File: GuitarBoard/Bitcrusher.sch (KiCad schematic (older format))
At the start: 20 parts, among them IC1 CD4069UBE, Q6 2N3904

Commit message: Finalized new guitar board
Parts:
- C10, C13: footprint Capacitor_THT:CP_Axial_L10.0mm_D6.0mm_P15.00mm_Horizontal -> Capacitor_THT:CP_Radial_D6.3mm_P2.50mm
- C11, C12, C6, C7, C8, C9: footprint libraries:C_Flat_L7.2_H6.5 -> Capacitor_THT:C_Rect_L7.2mm_W2.5mm_P5.00mm_FKS2_FKP2_MKS2_MKP2
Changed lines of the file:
@@
 F 0 "C6" V 798 2550 50  0000 C CNN
 F 1 "0.1uF" V 889 2550 50  0000 C CNN
-F 2 "libraries:C_Flat_L7.2_H6.5" H 1088 2400 50  0001 C CNN
+F 2 "Capacitor_THT:C_Rect_L7.2mm_W2.5mm_P5.00mm_FKS2_FKP2_MKS2_MKP2" H 1088 2400 50  0001 C CNN
 F 3 "~" H 1050 2550 50  0001 C CNN
 	1    1050 2550
@@
 F 0 "C7" V 1298 2000 50  0000 C CNN
 F 1 "2200pF" V 1389 2000 50  0000 C CNN
-F 2 "libraries:C_Flat_L7.2_H6.5" H 1588 1850 50  0001 C CNN
+F 2 "Capacitor_THT:C_Rect_L7.2mm_W2.5mm_P5.00mm_FKS2_FKP2_MKS2_MKP2" H 1588 1850 50  0001 C CNN
 F 3 "~" H 1550 2000 50  0001 C CNN
 	1    1550 2000
@@
 F 0 "C8" V 1798 2550 50  0000 C CNN
 F 1 "0.1uF" V 1889 2550 50  0000 C CNN
-F 2 "libraries:C_Flat_L7.2_H6.5" H 2088 2400 50  0001 C CNN
+F 2 "Capacitor_THT:C_Rect_L7.2mm_W2.5mm_P5.00mm_FKS2_FKP2_MKS2_MKP2" H 2088 2400 50  0001 C CNN
 F 3 "~" H 2050 2550 50  0001 C CNN
 	1    2050 2550
@@
 F 0 "C9" V 2298 2000 50  0000 C CNN
 F 1 "4700pF" V 2389 2000 50  0000 C CNN
-F 2 "libraries:C_Flat_L7.2_H6.5" H 2588 1850 50  0001 C CNN
+F 2 "Capacitor_THT:C_Rect_L7.2mm_W2.5mm_P5.00mm_FKS2_FKP2_MKS2_MKP2" H 2588 1850 50  0001 C CNN
 F 3 "~" H 2550 2000 50  0001 C CNN
 	1    2550 2000
@@
 F 0 "C11" V 4398 2300 50  0000 C CNN
 F 1 "100pF" V 4489 2300 50  0000 C CNN
-F 2 "libraries:C_Flat_L7.2_H6.5" H 4688 2150 50  0001 C CNN
+F 2 "Capacitor_THT:C_Rect_L7.2mm_W2.5mm_P5.00mm_FKS2_FKP2_MKS2_MKP2" H 4688 2150 50  0001 C CNN
 F 3 "~" H 4650 2300 50  0001 C CNN
 	1    4650 2300
@@
 F 0 "C13" V 7455 2650 50  0000 C CNN
 F 1 "10uF" V 7364 2650 50  0000 C CNN
-F 2 "Capacitor_THT:CP_Axial_L10.0mm_D6.0mm_P15.00mm_Horizontal" H 7238 2500 50  0001 C CNN
+F 2 "Capacitor_THT:CP_Radial_D6.3mm_P2.50mm" H 7238 2500 50  0001 C CNN
 F 3 "~" H 7200 2650 50  0001 C CNN
 	1    7200 2650
@@
 F 0 "C12" H 6100 3300 50  0000 C CNN
 F 1 "1000pF" H 6100 3400 50  0000 C CNN
-F 2 "libraries:C_Flat_L7.2_H6.5" H 6288 3150 50  0001 C CNN
+F 2 "Capacitor_THT:C_Rect_L7.2mm_W2.5mm_P5.00mm_FKS2_FKP2_MKS2_MKP2" H 6288 3150 50  0001 C CNN
 F 3 "~" H 6250 3300 50  0001 C CNN
 	1    6250 3300
@@
 F 0 "C10" H 3718 3646 50  0000 L CNN
 F 1 "10uF" H 3718 3555 50  0000 L CNN
-F 2 "Capacitor_THT:CP_Axial_L10.0mm_D6.0mm_P15.00mm_Horizontal" H 3638 3450 50  0001 C CNN
+F 2 "Capacitor_THT:CP_Radial_D6.3mm_P2.50mm" H 3638 3450 50  0001 C CNN
 F 3 "~" H 3600 3600 50  0001 C CNN
 	1    3600 3600

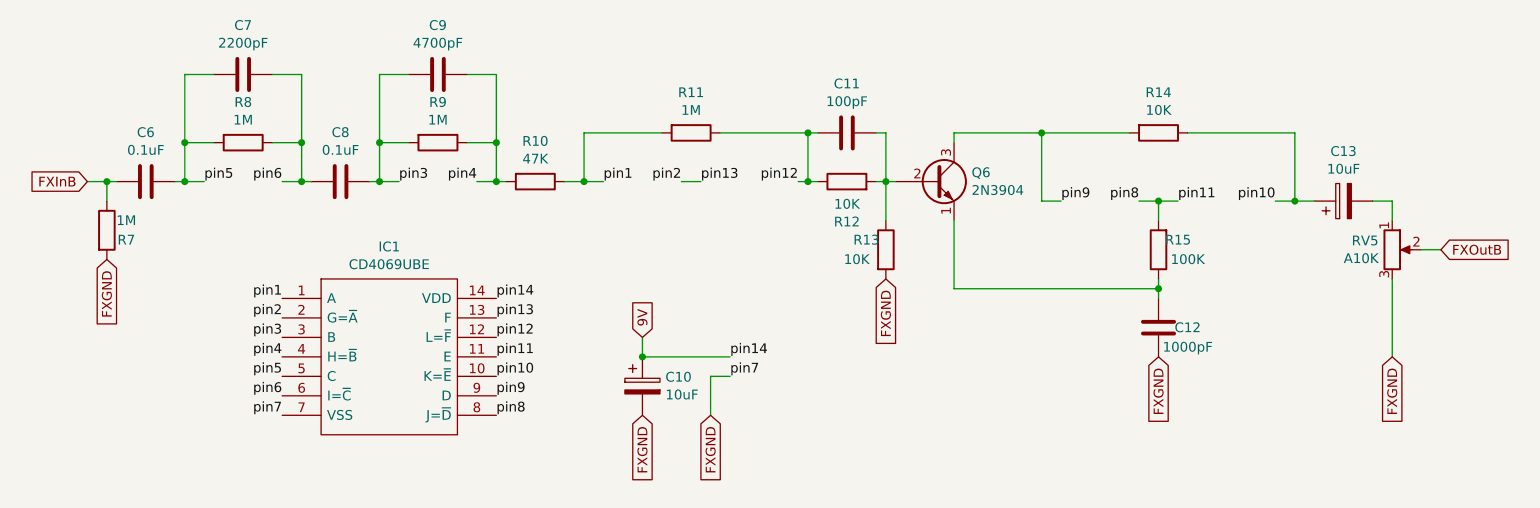
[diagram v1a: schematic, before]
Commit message: Fixed minor issues and reduced board size
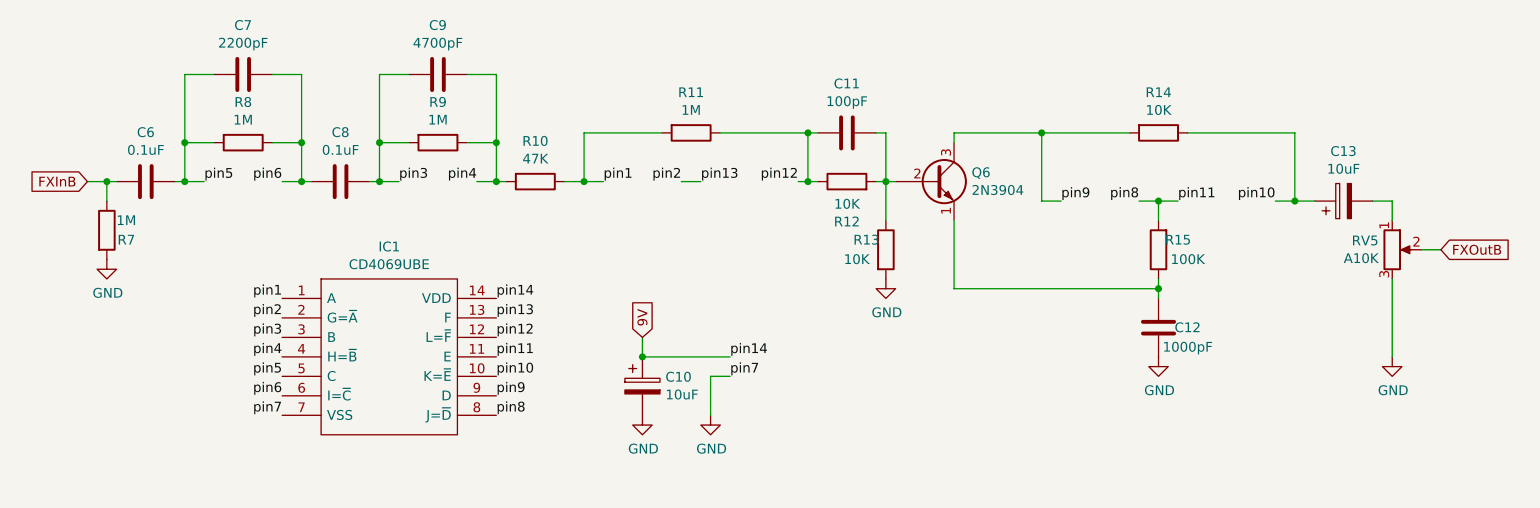
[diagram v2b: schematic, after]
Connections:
- net FXGND renamed GND
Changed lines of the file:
@@
 	3600 3350 3600 3450
 Connection ~ 3600 3450
-Text GLabel 850  2950 3    50   Input ~ 0
-FXGND
-Text GLabel 3950 3750 3    50   Input ~ 0
-FXGND
-Text GLabel 3600 3750 3    50   Input ~ 0
-FXGND
-Text GLabel 4850 3050 3    50   Input ~ 0
-FXGND
-Text GLabel 6250 3450 3    50   Input ~ 0
-FXGND
-Text GLabel 7450 3450 3    50   Input ~ 0
-FXGND
+$Comp
+L power:GND #PWR0106
+U 1 1 61CEB8FC
+P 3950 3750
+F 0 "#PWR0106" H 3950 3500 50  0001 C CNN
+F 1 "GND" H 3955 3577 50  0000 C CNN
+F 2 "" H 3950 3750 50  0001 C CNN
+F 3 "" H 3950 3750 50  0001 C CNN
+	1    3950 3750
+	1    0    0    -1
+$EndComp
+$Comp
+L power:GND #PWR0107
+U 1 1 61CED2D6
+P 3600 3750
+F 0 "#PWR0107" H 3600 3500 50  0001 C CNN
+F 1 "GND" H 3605 3577 50  0000 C CNN
+F 2 "" H 3600 3750 50  0001 C CNN
+F 3 "" H 3600 3750 50  0001 C CNN
+	1    3600 3750
+	1    0    0    -1
+$EndComp
+$Comp
+L power:GND #PWR0108
+U 1 1 61CEDDB0
+P 850 2950
+F 0 "#PWR0108" H 850 2700 50  0001 C CNN
+F 1 "GND" H 855 2777 50  0000 C CNN
+F 2 "" H 850 2950 50  0001 C CNN
+F 3 "" H 850 2950 50  0001 C CNN
+	1    850  2950
+	1    0    0    -1
+$EndComp
+$Comp
+L power:GND #PWR0109
+U 1 1 61CEE9A7
+P 4850 3050
+F 0 "#PWR0109" H 4850 2800 50  0001 C CNN
+F 1 "GND" H 4855 2877 50  0000 C CNN
+F 2 "" H 4850 3050 50  0001 C CNN
+F 3 "" H 4850 3050 50  0001 C CNN
+	1    4850 3050
+	1    0    0    -1
+$EndComp
+$Comp
+L power:GND #PWR0110
+U 1 1 61CEFB97
+P 6250 3450
+F 0 "#PWR0110" H 6250 3200 50  0001 C CNN
+F 1 "GND" H 6255 3277 50  0000 C CNN
+F 2 "" H 6250 3450 50  0001 C CNN
+F 3 "" H 6250 3450 50  0001 C CNN
+	1    6250 3450
+	1    0    0    -1
+$EndComp
+$Comp
+L power:GND #PWR0111
+U 1 1 61CF06D8
+P 7450 3450
+F 0 "#PWR0111" H 7450 3200 50  0001 C CNN
+F 1 "GND" H 7455 3277 50  0000 C CNN
+F 2 "" H 7450 3450 50  0001 C CNN
+F 3 "" H 7450 3450 50  0001 C CNN
+	1    7450 3450
+	1    0    0    -1
+$EndComp
 $EndSCHEMATC
